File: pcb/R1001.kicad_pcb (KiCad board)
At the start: 4 copper layers, 45 x 33.3 mm, 31 parts, among them J1 PCIEXPRESS-X1, J2 CONN_01X04, U1 DRV8825, U2 74LS157, U3 EFM8BB10F2G

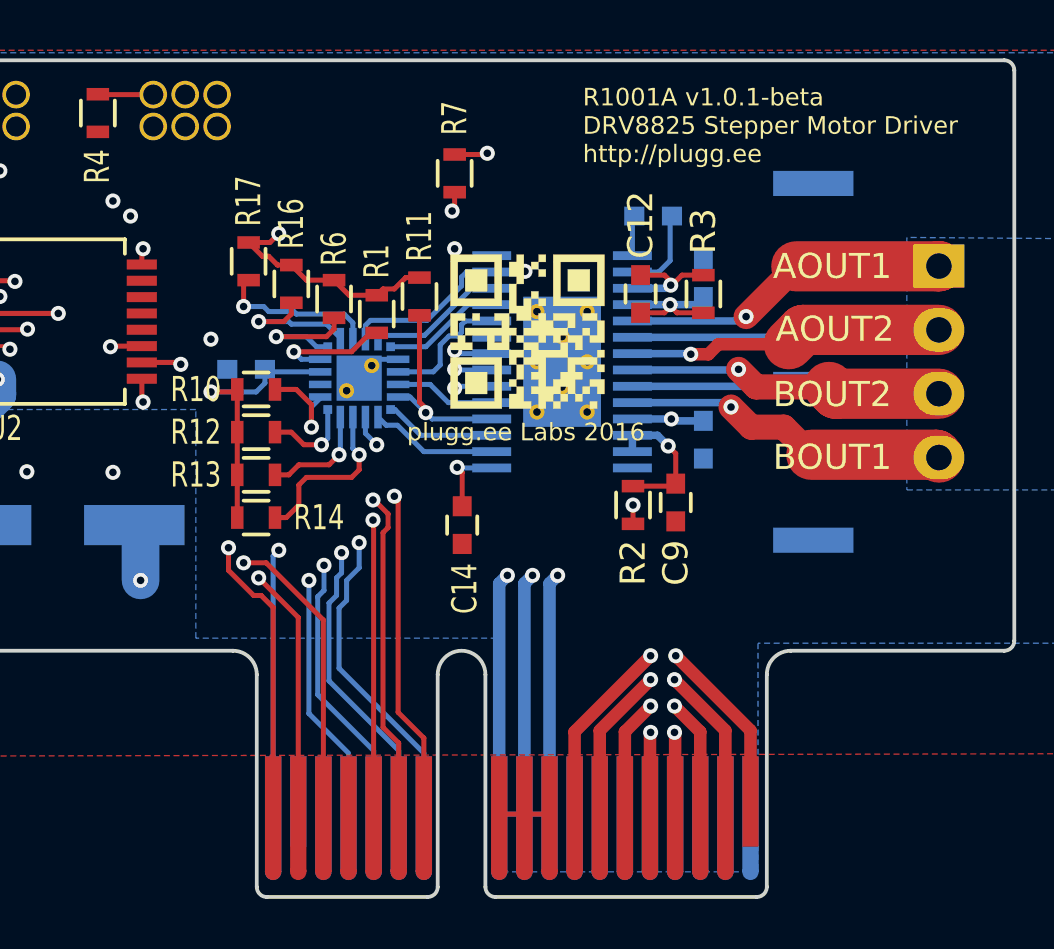
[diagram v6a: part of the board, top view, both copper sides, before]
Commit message: released 1.02 beta to adjust assign busy bee I2C pins to 0.0 and 0.1
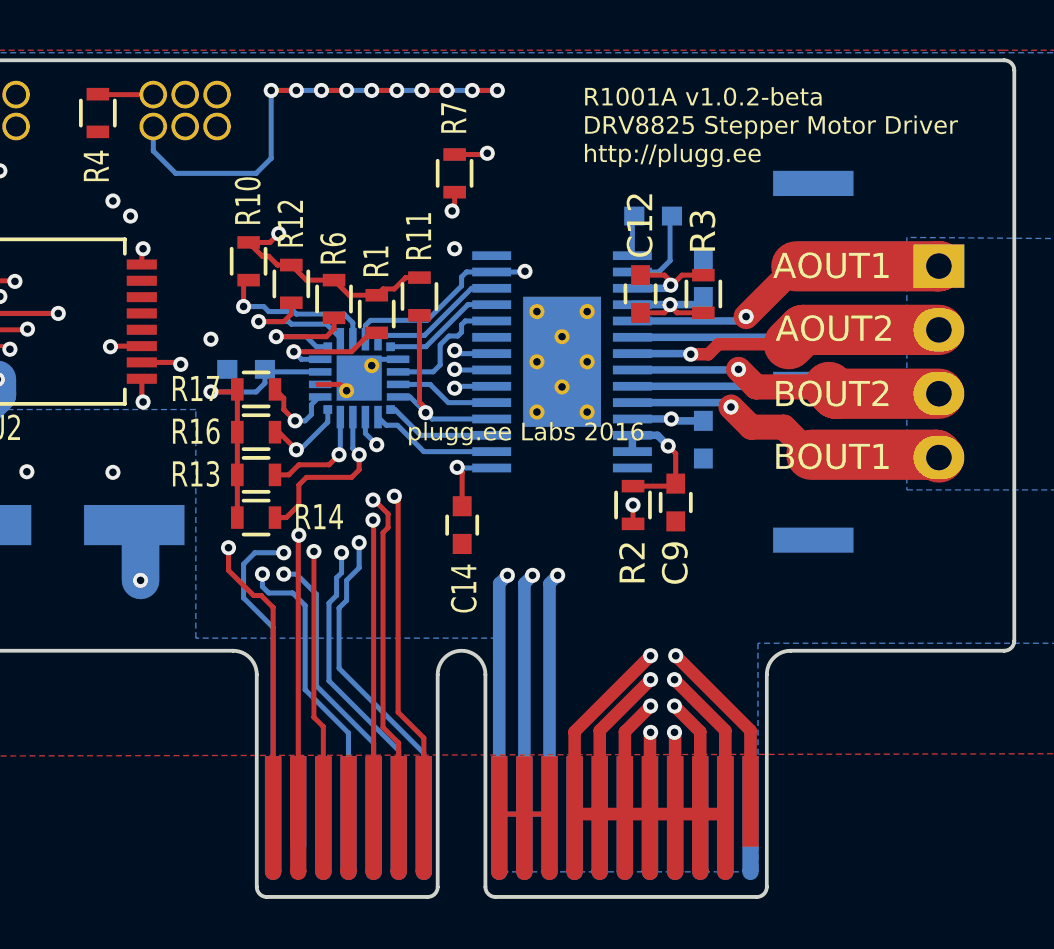
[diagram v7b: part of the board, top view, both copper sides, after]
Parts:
- removed G***: LOGO, pluggee:pluggee-QRNEG-085X085
- moved R12 6.06 mm to (141.2, 78.9), turned to 270 degrees
- moved R16 6.06 mm to (139.8, 84.8), turned to 0 degrees
- moved R10 5.11 mm to (139.5, 78.0), turned to 270 degrees
- moved R17 5.11 mm to (139.8, 83.1), turned to 0 degrees
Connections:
- U3 pad 1: ID2 -> SDA
- U3 pad 2: ID3 -> SCL
- U3 pad 7: SDA -> ID2
- U3 pad 8: SCL -> ID3
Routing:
- net GND: track 28.1 -> 47.4 mm, vias 1 -> 11
- net SCL: track 30.7 -> 21.9 mm
- net ID3: track 22.5 -> 31.2 mm
- net ID2: track 21.6 -> 29.5 mm
- net SDA: track 28.0 -> 20.3 mm
- net HT: track 117.6 -> 123.6 mm
- net C2D: track 26.5 -> 28.3 mm
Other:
- board text added: "R1001A v1.0.2-beta DRV8825 Stepper Motor Driver http://plugg.ee"
- board text removed: "R1001A v1.0.1-beta DRV8825 Stepper Motor Driver http://plugg.ee"

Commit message: wip
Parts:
- added J3: CONN127P-02X02, Main:CONN127P-02X02, F.Cu at (151.0, 72.0)
- added Q1: Q_NMOS_GSD, Main:SOT190P290X130X100-3, F.Cu at (153.6, 109.7)
- added R15: R1206, Main:RESC1206, F.Cu at (155.1, 114.3)
- added R18: R0603, Main:RESC0603, F.Cu at (146.7, 118.9)
- added R19: 1k, Resistors_SMD:R_0603, F.Cu at (139.3, 110.3)
- added R20: R0603, Main:RESC0603, F.Cu at (139.4, 117.6)
- added R21: R0603, Main:RESC0603, F.Cu at (148.6, 114.6)
- added R8: 1k, Resistors_SMD:R_0603, F.Cu at (138.7, 114.6)
- added U4: ZXCT1107, Main:SOT190P290X130X100-3, F.Cu at (144.4, 108.8)
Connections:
- J1 pad A1: HT -> /HT_CON
- J1 pad A18: ~MRESET -> /~MRESET_CON
- J1 pad A2: HT -> /HT_CON
- J1 pad A3: HT -> /HT_CON
- J1 pad A4: HT -> /HT_CON
- J1 pad A5: HT -> /HT_CON
- J1 pad A6: HT -> /HT_CON
- J1 pad A7: HT -> /HT_CON
- J1 pad A8: HT -> /HT_CON
- J1 pad B18: C2D -> /C2D_CON
- JMASTER1 pad 1: PX3_STEP -> /STEP
- JMASTER1 pad 2: PX2_~ENBL -> /~ENBL
- JMASTER1 pad 3: PX1_DIR -> /DIR
- U1 pad 17: /~MCU_SLEEP -> +3V3
- U3 pad 16: /~MCU_SLEEP -> /IVDD_SENSE
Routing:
- net HT: track 123.6 -> 14.0 mm, vias 11 -> 2
- net PX2_~ENBL: track 48.5 -> 2.30 mm, vias 3 -> 0
- net PX3_STEP: track 47.6 -> 4.13 mm, vias 3 -> 0
- net ~MRESET: track 32.6 -> 7.89 mm, vias 2 -> 1
- net /~MRESET_CON: track 0.00 -> 24.7 mm, vias 0 -> 1
- net /HT_CON: track 0.00 -> 22.1 mm
- net GND: track 47.4 -> 29.4 mm, vias 11 -> 1
- net PX1_DIR: track 47.3 -> 33.8 mm, vias 4 -> 3
- net /C2D_CON: track 0.00 -> 13.4 mm
- net C2D: track 28.3 -> 15.0 mm
- net /STEP: track 26.8 -> 33.0 mm, vias 3 -> 4
- net /~MCU_SLEEP: track 4.45 -> 0.00 mm
- net +3V3: track 66.0 -> 68.8 mm
- net /IVDD_SENSE: track 0.00 -> 1.62 mm
- net /~ENBL: track 24.3 -> 24.8 mm
